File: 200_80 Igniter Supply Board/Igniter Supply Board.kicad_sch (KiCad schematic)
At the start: 0 parts

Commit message: Ignitier schematic first pass
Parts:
- added C10, C11, C13, C9: 470pF, symbol Device:C
- added C12, C6: 1pF, symbol Device:C
- added C14, C16, C18, C20, C22, C24, C4: 100nF, symbol Device:C
- added C15, C17, C19, C21, C23, C25, C5, C7: 1nF, symbol Device:C
- added C2: 10uF, symbol Device:C
- added C3: 10uF, symbol Device:C_US
- added C8: 1uF, symbol Device:C_Polarized_US
- added D1, D3, D5: BAT54L, symbol Device:D_Schottky
- added D2: SZBZX84C18LT3G, symbol Device:D_Zener
- added D4, D6: MMSZ4685, symbol Device:D_Zener
- added J1, J2: BNC, symbol Connector:Conn_Coaxial
- added J3: Picoblade, symbol Connector:Conn_01x07_Socket
- added Q1: G2R1000MT33J-TR, Package_TO_SOT_SMD:TO-263-7_TabPin8, symbol Transistor_FET:C2M1000170J
- added R1: 0R, symbol Device:R_US
- added R2: DNP, symbol Device:R_US
- added R3: 165k, symbol Device:R_US
- added R4, R6: 4.53M, symbol Device:R_US
- added R5, R7: 10k, symbol Device:R_US
- added T1: 750319697, symbol Device:Transformer_SP_1S
- added U1, U2, U3: OP37, symbol 0_PAY_Symbol_Library:OP37
- added U4: ISO7220MDR, Package_SO:SOIC-8_3.9x4.9mm_P1.27mm, symbol Isolator:ISO6720BD
- added U5: LT8301, Package_TO_SOT_SMD:TSOT-23-5, symbol Regulator_Switching:LT8303
- added U6: (no value), symbol 0_PAY_Symbol_Library:ACS37042KLHBLT-030B3
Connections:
- new net: C2.1, C4.1, C5.1, D1.1 (K), U4.8 (VCC2)
- new net: C2.2, C4.2, C5.2, D2.2 (A), Q1.2 (DS), R2.1, T1.6 (S2), U4.5 (GND2)
- new net: R3.2, T1.3 (PR2), U5.4 (SW)
- new net: D1.2 (A), T1.4 (S1)
- new net: C6.1, C8.1, J1.1 (In), Q1.3 (S), Q1.4 (S), Q1.5 (S), Q1.6 (S), Q1.7 (S), R4.2
- new net: D2.1 (K), Q1.1 (G), R1.2, R2.2
- new net: C11.1, C12.2, C13.1, R6.1, R7.2, U2.2 (-)
- new net: C12.1, J2.1 (In), Q1.8 (D), R6.2
- new net: J2.2 (Ext), U6.4 (IP+)
- new net: U3.3 (+), U6.2 (VOUT)
- new net: R1.1, U4.7 (OUTA)
- new net: C10.1, C6.2, C9.1, R4.1, R5.2, U1.2 (-)
- new net: R3.1, U5.3 (RFB)
- new net -5V: C20.2, C21.2, C22.2, C23.2, C24.2, C25.2, J3.2 (Pin_2), U1.4 (V-), U2.4 (V-), U3.4 (V-)
- new net 5V: C14.1, C15.1, C16.1, C17.1, C18.1, C19.1, C3.1, C7.1, J3.3 (Pin_3), T1.1 (PR1), U1.7 (V+), U2.7 (V+), U3.7 (V+), U4.1 (VCC1), U5.1 (EN/UVLO), U5.5 (VIN), U6.3 (VDD)
- new net GND: C10.2, C11.2, C14.2, C15.2, C16.2, C17.2, C18.2, C19.2, C20.1, C21.1, C22.1, C23.1, C24.1, C25.1, C3.2, C7.2, D3.2 (A), D4.2 (A), D5.2 (A), D6.2 (A), J3.1 (Pin_1), U1.3 (+), U2.3 (+), U4.4 (GND1), U5.2 (GND), U6.1 (GND)
- new net GNDPWR: C8.2, J1.2 (Ext), U6.5 (IP-)
- new net IG_SupV: J3.4 (Pin_4)
- new net IgniterI: J3.6 (Pin_6), U3.2 (-), U3.6
- new net IgniterV: C13.2, C9.2, D3.1 (K), D4.1 (K), D5.1 (K), D6.1 (K), J3.5 (Pin_5), R5.1, R7.1, U1.6, U2.6
- new net PulseIn: J3.7 (Pin_7), U4.2 (INA)
- no-connect marks 0 -> 13
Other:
- note added: "-1 kV Input"
- note added: "Arbitrary output capacitance rn"
- note added: "Can design a better amplifier later"
- note added: "Igniter Output"
- note added: "Reference to regular ground because I- can vary by ~3V (1R hall sensor) which would fuck up the divider, tank the systematic error of a couple millivolts"
- note added: "Vout=100u(Rfb/N)-Vd"

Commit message: I'm still making progress
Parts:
- removed C7: 1nF, symbol Device:C
- removed J3: Picoblade, symbol Connector:Conn_01x07_Socket
- removed U4: ISO7220MDR, Package_SO:SOIC-8_3.9x4.9mm_P1.27mm, symbol Isolator:ISO6720BD
- added C26: 100nF, symbol Device:C
- added C27: 1nF, symbol Device:C
- added C28, C29: 10uF, symbol Device:C
- added D7: BAT54L, symbol Device:D_Schottky
- added D8: MMSZ4685, symbol Device:D_Zener
- added J3: 53261-1371, symbol Connector:Conn_01x13_Socket
- added R10, R8: 1k, symbol Device:R_US
- added R11: 2.7k, symbol Device:R_US
- added R12: 83R, symbol Device:R_US
- added R9: 2.5k, symbol Device:R_US
- added TH1: Thermistor_NTC_US, symbol Device:Thermistor_NTC_US
- added U7: Si8261BAC, Package_SO:SSO-6_6.8x4.6mm_P1.27mm_Clearance7mm, symbol Driver_FET:ACPL-P343
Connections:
- net -5V: now also C29.2, J3.7 (Pin_7), R11.1
- net 5V: now also C26.1, C27.1, C28.1, J3.6 (Pin_6)
- net GND: now also C26.2, C27.2, C28.2, C29.1, D7.2 (A), D8.2 (A), J3.3 (Pin_3), J3.4 (Pin_4), J3.5 (Pin_5), R10.2, TH1.2, U7.3 (C)
- net at C2.1, C4.1, C5.1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: now also U7.6 (VCC)
- net at C2.2, C4.2, C5.2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: now also U7.4 (VEE)
- net at U3.3 (+): now also R11.2, R8.1; no longer U6.2 (VOUT)
- net at R1.1: now also U7.5 (VO)
- net IgniterI: no longer names the net of U3.2 (-)
- net IgniterI: now also R10.1, R9.1; no longer U3.6
- net IgniterV renamed ADC_V_IGN_PK
- net ADC_V_IGN_PK: now also J3.9 (Pin_9); no longer C9.2, D3.1 (K), D4.1 (K), R5.1, U1.6
- new net: R8.2, U6.2 (VOUT)
- new net: R12.1, U7.1 (A)
- new net ADC_I_IGN_PK: D7.1 (K), D8.1 (K), J3.10 (Pin_10), R9.2, U3.6
- new net ADC_NTC_IGN: J3.11 (Pin_11), TH1.1
- new net ADC_V_IGN_SUPPLY: C9.2, D3.1 (K), D4.1 (K), J3.8 (Pin_8), R5.1, U1.6
- new net IGNITER_PULSE: J3.13 (Pin_13), R12.2
- new net IGNITER_RST: J3.12 (Pin_12)
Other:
- note added: "Designed for 6mA at 2.8V Vf with 3.3V input"
- note added: "Put thermistors here"
- note added: "Scales first to 0-3.3"
- note removed: "Can design a better amplifier later"
- moved on the sheet: C14, C15, C16, C17, C18, C19, C20, C21, C22, C23, C24, C25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

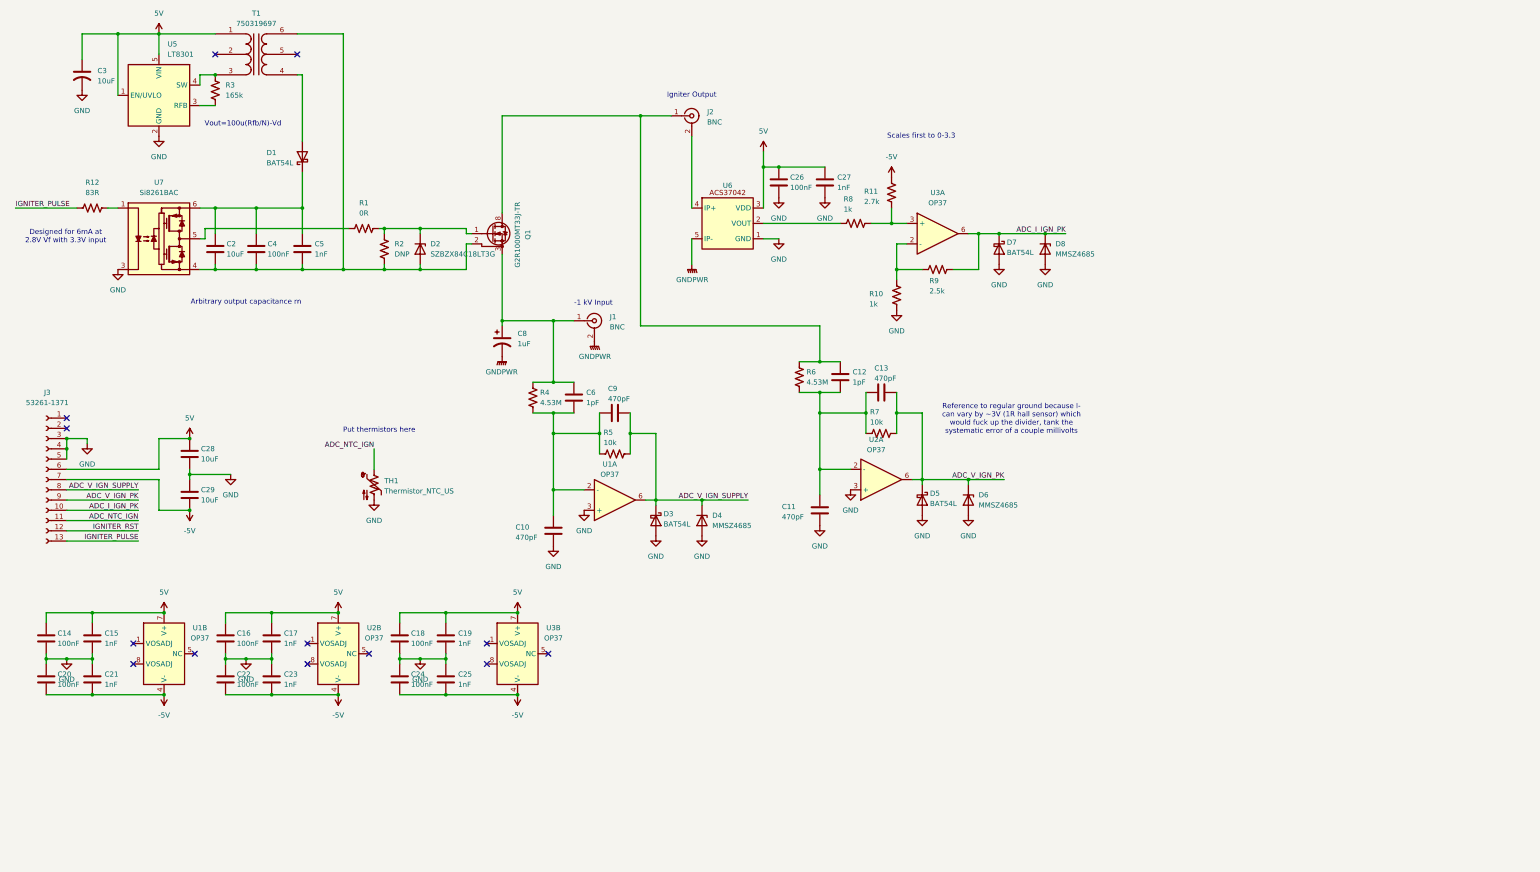
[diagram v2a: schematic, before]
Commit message: Igniter schematic finished, moving to layout
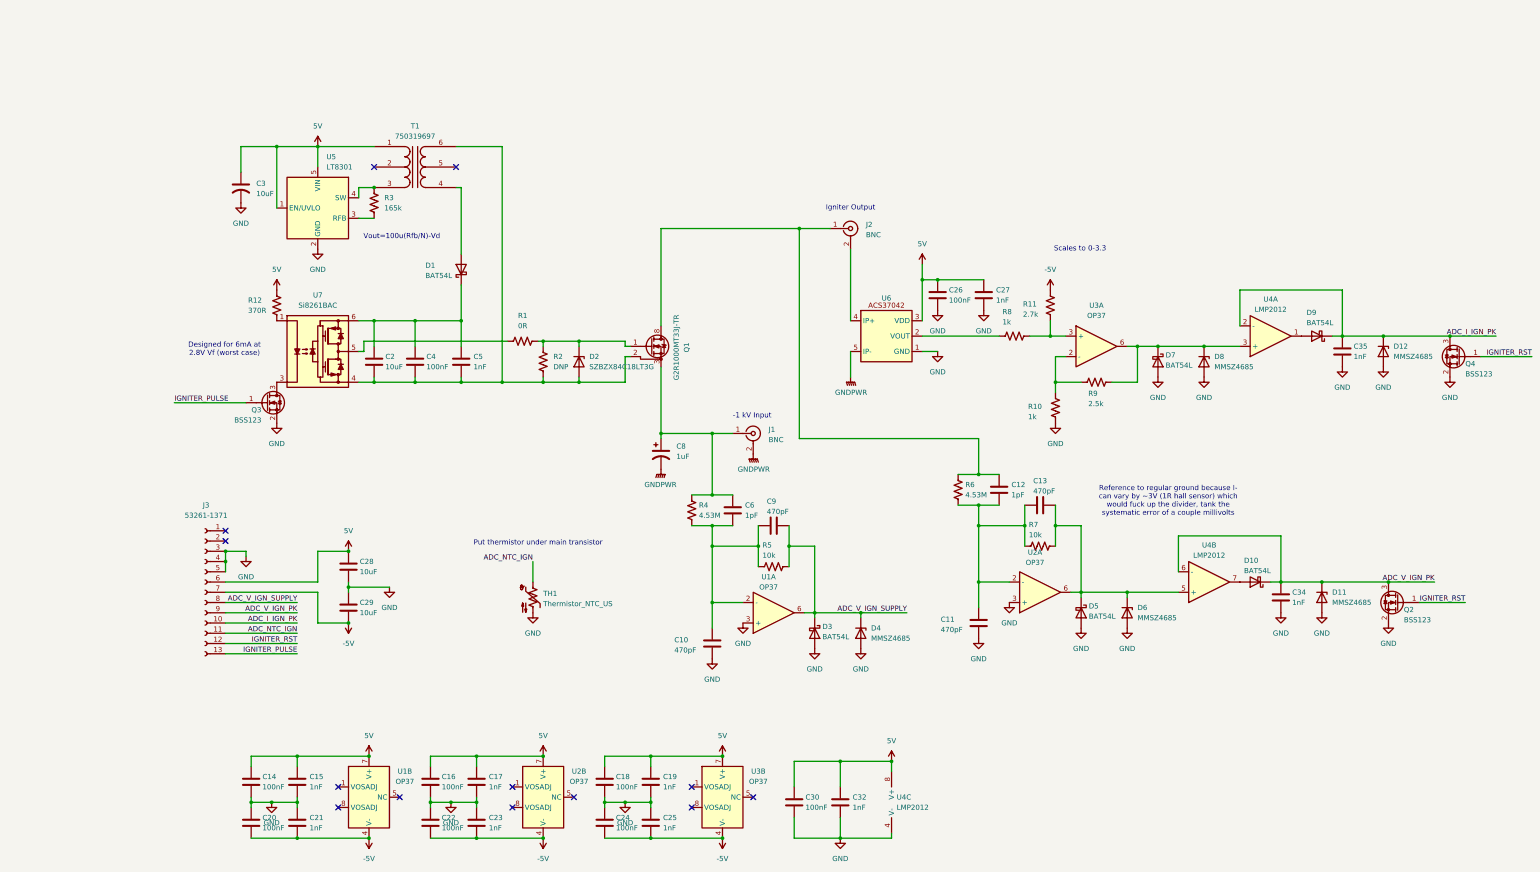
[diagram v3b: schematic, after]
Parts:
- added C30: 100nF, symbol Device:C
- added C32, C34, C35: 1nF, symbol Device:C
- added D10, D9: BAT54L, symbol Device:D_Schottky
- added D11, D12: MMSZ4685, symbol Device:D_Zener
- added Q2, Q3, Q4: BSS123, Package_TO_SOT_SMD:SOT-23, symbol Transistor_FET:BSS123
- added U4: LMP2012, symbol Device:Opamp_Dual
- R12: value 83R -> 370R
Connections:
- net 5V: now also R12.2, C30.1, C32.1, U4.8 (V+)
- net ADC_I_IGN_PK: now also C35.1, D12.1 (K), D9.1 (K), Q4.3 (D), U4.2 (-); no longer D7.1 (K), D8.1 (K), R9.2, U3.6
- net ADC_V_IGN_PK: now also C34.1, D10.1 (K), D11.1 (K), Q2.3 (D), U4.6 (-); no longer C13.2, D5.1 (K), D6.1 (K), R7.1, U2.6
- net GND: now also C30.2, C32.2, C34.2, C35.2, D11.2 (A), D12.2 (A), Q2.2 (S), Q3.2 (S), Q4.2 (S), U4.4 (V-); no longer U7.3 (C)
- net IGNITER_PULSE: now also Q3.1 (G); no longer R12.2
- net IGNITER_RST: now also Q2.1 (G), Q4.1 (G)
- new net: C13.2, D5.1 (K), D6.1 (K), R7.1, U2.6, U4.5 (+)
- new net: D7.1 (K), D8.1 (K), R9.2, U3.6, U4.3 (+)
- new net: D10.2 (A), U4.7
- new net: D9.2 (A), U4.1
- new net: Q3.3 (D), U7.3 (C)
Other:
- note added: "Designed for 6mA at 2.8V Vf (worst case)"
- note added: "Put thermistor under main transistor"
- note added: "Scales to 0-3.3"
- note removed: "Arbitrary output capacitance rn"
- note removed: "Designed for 6mA at 2.8V Vf with 3.3V input"
- note removed: "Put thermistors here"
- note removed: "Scales first to 0-3.3"
- moved on the sheet: C10, C11, C12, C13, C14, C15, C16, C17, C18, C19, C2, C20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

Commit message: Igniter PCB floorplan
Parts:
- removed C3: 10uF, symbol Device:C_US
- added C31: 10uF, Capacitor_SMD:C_1210_3225Metric_Pad1.33x2.70mm_HandSolder, symbol Device:C
- added D13, D16: PESD3V3U1UL, Diode_SMD:D_SOD-882, symbol Diode:PESD3V3U1UL
- added D14, D15: PESD5V0S1UL, Diode_SMD:D_SOD-882, symbol Diode:PESD5V0S1UL
- added TP1, TP2, TP3, TP4, TP5, TP6: TestPoint_Alt, symbol Connector:TestPoint_Alt
- C10, C11, C13, C9: footprint (none) -> Capacitor_SMD:C_1206_3216Metric_Pad1.33x1.80mm_HandSolder
- C12, C6: footprint (none) -> Capacitor_SMD:C_2225_5664Metric_Pad1.80x6.60mm_HandSolder
- C14, C15, C16, C17, C18, C19, C20, C21, C22, C23, C24, C25, C26, C27, C30, C32, C34, C35, C4, C5: footprint (none) -> Capacitor_SMD:C_0603_1608Metric_Pad1.08x0.95mm_HandSolder
- C2, C28, C29: footprint (none) -> Capacitor_SMD:C_1210_3225Metric_Pad1.33x2.70mm_HandSolder
- C8: footprint (none) -> Capacitor_THT:C_Rect_L33.0mm_W20.0mm_P27.50mm_MKS4
- D1, D10, D3, D5, D7, D9: footprint (none) -> Package_TO_SOT_SMD:SOT-23-3
- D11, D12, D4, D6, D8: footprint (none) -> Diode_SMD:D_SOD-123
- D2: footprint (none) -> Package_TO_SOT_SMD:SOT-23_Handsoldering
- J1, J2: footprint (none) -> CONN_73138-5033_MOL
- J3: footprint (none) -> Connector_Molex:Molex_PicoBlade_53398-1371_1x13-1MP_P1.25mm_Vertical
- R1, R10, R11, R12, R2, R3, R4, R5, R6, R7, R8, R9: footprint (none) -> Resistor_SMD:R_0603_1608Metric_Pad0.98x0.95mm_HandSolder
- T1: footprint (none) -> 0_PAY_Footprint_Library:Transformer_Wuerth_750319697
- TH1: value Thermistor_NTC_US -> NCU18XH103F60RB; footprint (none) -> Resistor_SMD:R_0603_1608Metric_Pad0.98x0.95mm_HandSolder
- U1, U2, U3, U4: footprint (none) -> Package_SO:SOIC-8_5.3x6.2mm_P1.27mm
- U6: footprint (none) -> Package_TO_SOT_SMD:TSOT-23-5_HandSoldering
- U7: footprint Package_SO:SSO-6_6.8x4.6mm_P1.27mm_Clearance7mm -> Package_SO:SOIC-8_5.3x6.2mm_P1.27mm
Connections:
- net GNDPWR is gone; now on net GND: C8.2, J1.2 (Ext), U6.5 (IP-)
- net -5V: now also D15.2 (A)
- net 5V: now also C31.1, D14.1 (K)
- net ADC_I_IGN_PK: now also D9.3 (K); no longer D9.1 (K)
- net ADC_V_IGN_PK: now also D10.3 (K); no longer D10.1 (K)
- net ADC_V_IGN_SUPPLY: now also D3.3 (K); no longer D3.1 (K)
- net GND: now also D3.1 (A), D5.1 (A), D7.1 (A), C31.2, D13.2 (A), D14.2 (A), D15.1 (K), D16.2 (A); no longer D3.2 (A), D5.2 (A), D7.2 (A)
- net IGNITER_PULSE: now also D16.1 (K)
- net IGNITER_RST: now also D13.1 (K)
- net at C2.1, C4.1, C5.1: now also D1.3 (K), U7.8 (VCC); no longer D1.1 (K), U7.6 (VCC)
- net at C2.2, C4.2, C5.2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: now also D2.1 (A), U7.5 (VEE), TP5.1; no longer D2.2 (A), U7.4 (VEE)
- net at T1.4 (S1): now also D1.1 (A), TP6.1; no longer D1.2 (A)
- net at C6.1, C8.1, J1.1 (In)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: now also TP3.1
- net at Q1.1 (G), R1.2, R2.2: now also D2.3 (K), TP4.1; no longer D2.1 (K)
- net at C13.2, D6.1 (K), R7.1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: now also D5.3 (K), U4.3 (+); no longer D5.1 (K), U4.5 (+)
- net at D8.1 (K), R9.2, U3.6: now also D7.3 (K), U4.5 (+); no longer D7.1 (K), U4.3 (+)
- net at C12.1, J2.1 (In), Q1.8 (D)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: now also TP2.1
- net at R8.2, U6.2 (VOUT): now also TP1.1
- net at U4.7: now also D10.1 (A); no longer D10.2 (A)
- net at U4.1: now also D9.1 (A); no longer D9.2 (A)
- net at R12.1: now also U7.2 (NC); no longer U7.1 (A)
- net at R1.1: now also U7.6 (VO), U7.7 (VO); no longer U7.5 (VO)
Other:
- note added: "TVS"
- moved on the sheet: C14, C15, C16, C17, C18, C19, C20, C21, C22, C23, C24, C25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

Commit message: Pushing for Alan
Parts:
- removed TP2, TP3: TestPoint_Alt, symbol Connector:TestPoint_Alt
- added C36, C39: 1nF, Capacitor_SMD:C_0603_1608Metric_Pad1.08x0.95mm_HandSolder, symbol Device:C
- added C37: 2.5nF, Capacitor_SMD:C_0603_1608Metric_Pad1.08x0.95mm_HandSolder, symbol Device:C
- added C38: 2.7nF, Capacitor_SMD:C_0603_1608Metric_Pad1.08x0.95mm_HandSolder, symbol Device:C
- added Q5: BSS123, Package_TO_SOT_SMD:SOT-23, symbol Transistor_FET:BSS123
- added R13: 10k, Resistor_SMD:R_0603_1608Metric_Pad0.98x0.95mm_HandSolder, symbol Device:R_US
- J1, J2: footprint CONN_73138-5033_MOL -> 0_PAY_Footprint_Library:CONN_112659
- R4, R6: footprint Resistor_SMD:R_0603_1608Metric_Pad0.98x0.95mm_HandSolder -> Resistor_SMD:R_2010_5025Metric_Pad1.40x2.65mm_HandSolder
- R5, R7: footprint Resistor_SMD:R_0603_1608Metric_Pad0.98x0.95mm_HandSolder -> Resistor_SMD:R_1206_3216Metric_Pad1.30x1.75mm_HandSolder
- TP1, TP4, TP5, TP6: value TestPoint_Alt -> 5015; footprint (none) -> TestPoint:TestPoint_Keystone_5015_Micro_Mini
- U4: value LMP2012 -> LMP2022
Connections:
- net -5V: now also C39.1
- net 5V: now also R13.1
- net GND: now also C37.1, Q5.2 (S)
- net IGNITER_RST: now also Q5.1 (G); no longer Q2.1 (G), Q4.1 (G)
- net at R11.2, R8.1, U3.3 (+): now also C38.1, C39.2
- net at C2.1, C4.1, C5.1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: now also TP6.1
- net at R10.1, R9.1, U3.2 (-): now also C36.2, C37.2
- net at D1.1 (A), T1.4 (S1): no longer TP6.1
- net at D7.3 (K), D8.1 (K), R9.2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: now also C36.1
- net at R8.2, TP1.1, U6.2 (VOUT): now also C38.2
- new net IGNITER_nRST: Q2.1 (G), Q4.1 (G), Q5.3 (D), R13.2
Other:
- moved on the sheet: C34, D10, D11, D7, D8, Q2, R10, R11, R8, R9, TP5, U3A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

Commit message: Fixed minor edits for Alan
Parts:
- removed J3: 53261-1371, Connector_Molex:Molex_PicoBlade_53398-1371_1x13-1MP_P1.25mm_Vertical, symbol Connector:Conn_01x13_Socket
- added J3: 53261-1371, Connector_Molex:Molex_PicoBlade_53398-1371_1x13-1MP_P1.25mm_Vertical, symbol Connector_Generic_MountingPin:Conn_01x13_MountingPin
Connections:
- net -5V: now also J3.6 (Pin_6)
- net 5V: now also J3.7 (Pin_7)
- net ADC_I_IGN_PK: now also J3.10 (Pin_10)
- net ADC_NTC_IGN: now also J3.11 (Pin_11)
- net ADC_V_IGN_PK: now also J3.9 (Pin_9)
- net ADC_V_IGN_SUPPLY: now also J3.8 (Pin_8)
- net GND: now also J3.3 (Pin_3), J3.4 (Pin_4), J3.5 (Pin_5), J3.MP (MountPin)
- net IGNITER_PULSE: now also J3.13 (Pin_13)
- net IGNITER_RST: now also J3.12 (Pin_12)

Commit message: Layout mostly done, gotta make claude happy now
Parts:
- removed D13, D16: PESD3V3U1UL, Diode_SMD:D_SOD-882, symbol Diode:PESD3V3U1UL
- removed D14, D15: PESD5V0S1UL, Diode_SMD:D_SOD-882, symbol Diode:PESD5V0S1UL
- added D13, D16, D17: MMSZ4685, Diode_SMD:D_SOD-123, symbol Device:D_Zener
- added D14, D15: MMSZ4690, Diode_SMD:D_SOD-123, symbol Device:D_Zener
- added R14: 10k, Resistor_SMD:R_0603_1608Metric_Pad0.98x0.95mm_HandSolder, symbol Device:R_US
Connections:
- net -5V: now also D15.2 (A)
- net 5V: now also D14.1 (K)
- net ADC_I_IGN_PK: now also J3.9 (Pin_9); no longer J3.10 (Pin_10)
- net ADC_NTC_IGN: now also D17.1 (K)
- net ADC_V_IGN_PK: now also J3.10 (Pin_10); no longer J3.9 (Pin_9)
- net GND: now also D13.2 (A), D14.2 (A), D15.1 (K), D16.2 (A), D17.2 (A), R14.2
- net IGNITER_PULSE: now also D16.1 (K), R14.1
- net IGNITER_RST: now also D13.1 (K)
- net at C13.2, D5.3 (K), D6.1 (K)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: now also U4.5 (+); no longer U4.3 (+)
- net at C36.1, D7.3 (K), D8.1 (K)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: now also U4.3 (+); no longer U4.5 (+)
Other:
- note added: "ESD Protection"
- note removed: "TVS"
- moved on the sheet: C34, C35, D10, D11, D12, D9, Q2, Q4, U4A, U4B

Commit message: Igniter board + discharge board first final draft
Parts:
- removed U4: LMP2022, Package_SO:SOIC-8_5.3x6.2mm_P1.27mm, symbol Device:Opamp_Dual
- added C33, C44, C46, C47, C48, C49: 100nF, Capacitor_SMD:C_0603_1608Metric_Pad1.08x0.95mm_HandSolder, symbol Device:C
- added C40, C41, C42: 500pF, Capacitor_SMD:C_0603_1608Metric_Pad1.08x0.95mm_HandSolder, symbol Device:C
- added C43, C45: 1nF, Capacitor_SMD:C_0603_1608Metric_Pad1.08x0.95mm_HandSolder, symbol Device:C
- added H1, H2, H3, H4: M2.5, MountingHole:MountingHole_2.7mm_M2.5_DIN965_Pad, symbol Mechanical:MountingHole_Pad
- added R15, R16, R17: 50R, Resistor_SMD:R_0603_1608Metric_Pad0.98x0.95mm_HandSolder, symbol Device:R_US
- added R18, R19: 100R, Resistor_SMD:R_0603_1608Metric_Pad0.98x0.95mm_HandSolder, symbol Device:R_US
- added U4: LMP2022MM, Package_SO:SOIC-8_5.3x6.2mm_P1.27mm, symbol 0_PAY_Symbol_Library:LMP2022
- added U8, U9: MAX997ESA, Package_SO:SOIC-8_3.9x4.9mm_P1.27mm, symbol Comparator:TLV3501AID
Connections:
- net 5V: now also C33.1, C43.1, C44.1, C45.1, U4.8 (V+), U8.7 (V+), U9.7 (V+)
- net ADC_I_IGN_PK: now also J3.10 (Pin_10), U4.6 (-), U4.7; no longer C35.1, D9.3 (K), J3.9 (Pin_9), Q4.3 (D)
- net ADC_V_IGN_PK: now also J3.9 (Pin_9), U4.1, U4.2 (-); no longer C34.1, D10.3 (K), J3.10 (Pin_10), Q2.3 (D)
- net ADC_V_IGN_SUPPLY: now also R15.1
- net GND: now also C33.2, C40.2, C41.2, C42.2, C43.2, C44.2, C45.2, C46.2, C47.2, C48.2, C49.2, U4.4 (V-), U8.4 (V-), U8.8 (SHDN), U9.4 (V-), U9.8 (SHDN)
- net at C13.2, D5.3 (K), D6.1 (K)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: now also R16.1, U9.2 (-)
- net at C36.1, D7.3 (K), D8.1 (K)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: now also R17.1, U8.2 (-)
- net at D9.1 (A): now also U8.6
- net at D10.1 (A): now also U9.6
- new net: C46.1, H1.1
- new net: C35.1, Q4.3 (D), R18.2, U4.5 (+), U8.3 (+)
- new net: C42.1, R17.2
- new net: C49.1, H4.1
- new net: C48.1, H3.1
- new net: C34.1, Q2.3 (D), R19.2, U4.3 (+), U9.3 (+)
- new net: C40.1, R15.2
- new net: C41.1, R16.2
- new net: D9.3 (K), R18.1
- new net: D10.3 (K), R19.1
- new net: C47.1, H2.1
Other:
- added sheet Discharge (Discharge.kicad_sch)
- moved on the sheet: C11, C12, C13, C14, C15, C16, C17, C18, C19, C20, C21, C22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
